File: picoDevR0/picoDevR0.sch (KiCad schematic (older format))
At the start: 10 parts, among them J1 Barrel_Jack, J2 Pico1to20, SW1 SW_Push_Dual, U1 LM1117-3.3

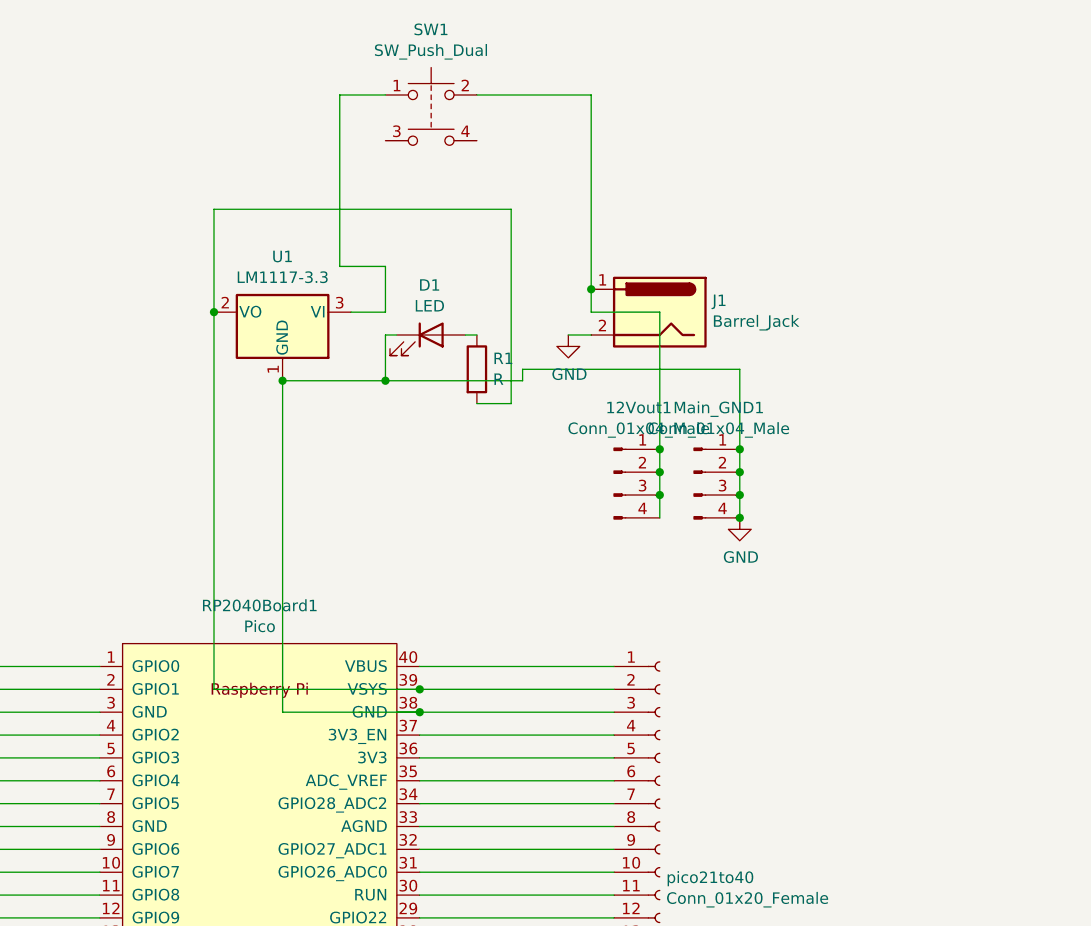
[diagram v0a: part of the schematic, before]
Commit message: added capacitors to LDO
and also made the sch more neat by adding 5V, 12V and GND labels.
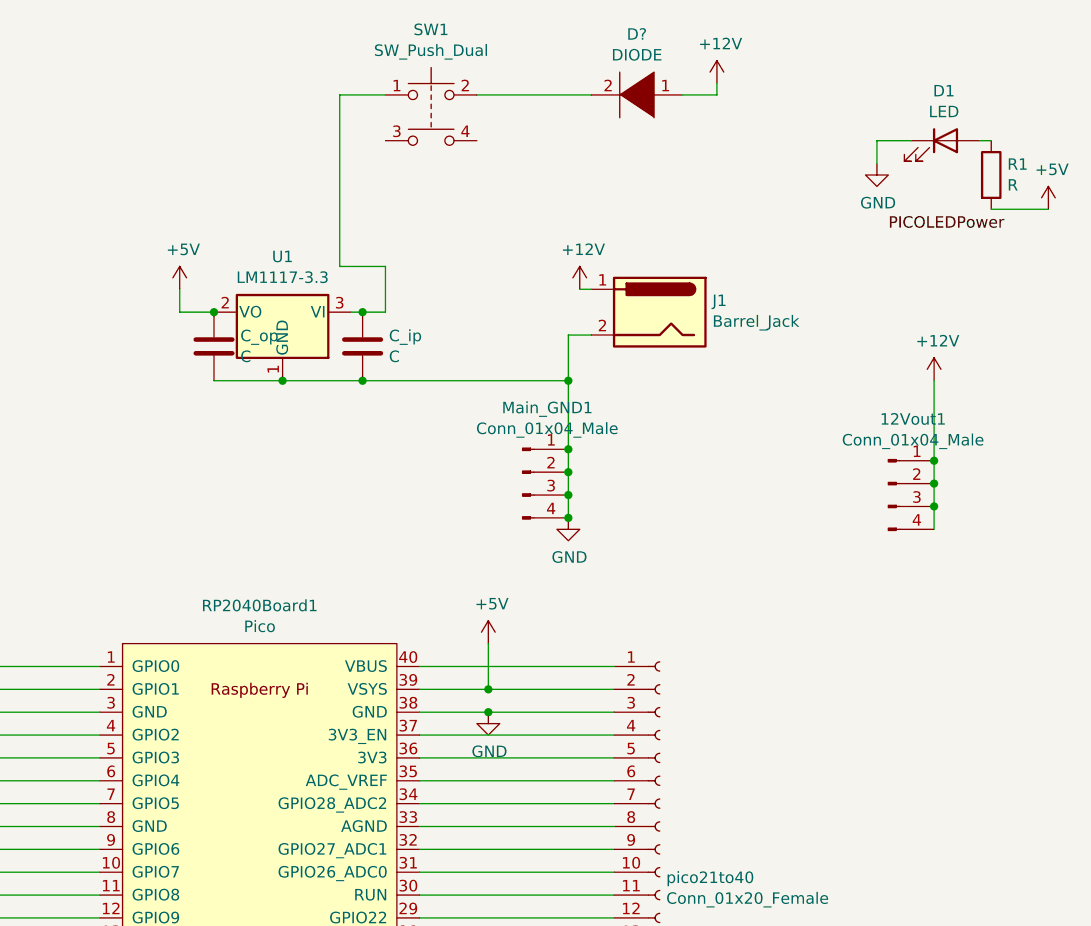
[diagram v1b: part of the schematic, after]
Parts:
- added C_ip, C_op: C, symbol Device:C
- added D?: DIODE, symbol pspice:DIODE
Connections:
- net GND: now also C_ip.2, C_op.2
- net +5V: now reaches R1.2, RP2040Board1.39 (VSYS), U1.2 (VO), pico21to40.2 (Pin_2)
- net +5V: now also C_op.1
- net at SW1.1, U1.3 (VI): now also C_ip.1
- net +12V: now reaches 12Vout1.1 (Pin_1), 12Vout1.2 (Pin_2), 12Vout1.3 (Pin_3), 12Vout1.4 (Pin_4), J1.1
- net +12V: now also D?.1 (K); no longer SW1.2
- new net: D?.2 (A), SW1.2
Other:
- moved on the sheet: 12Vout1, D1, Main_GND1, R1

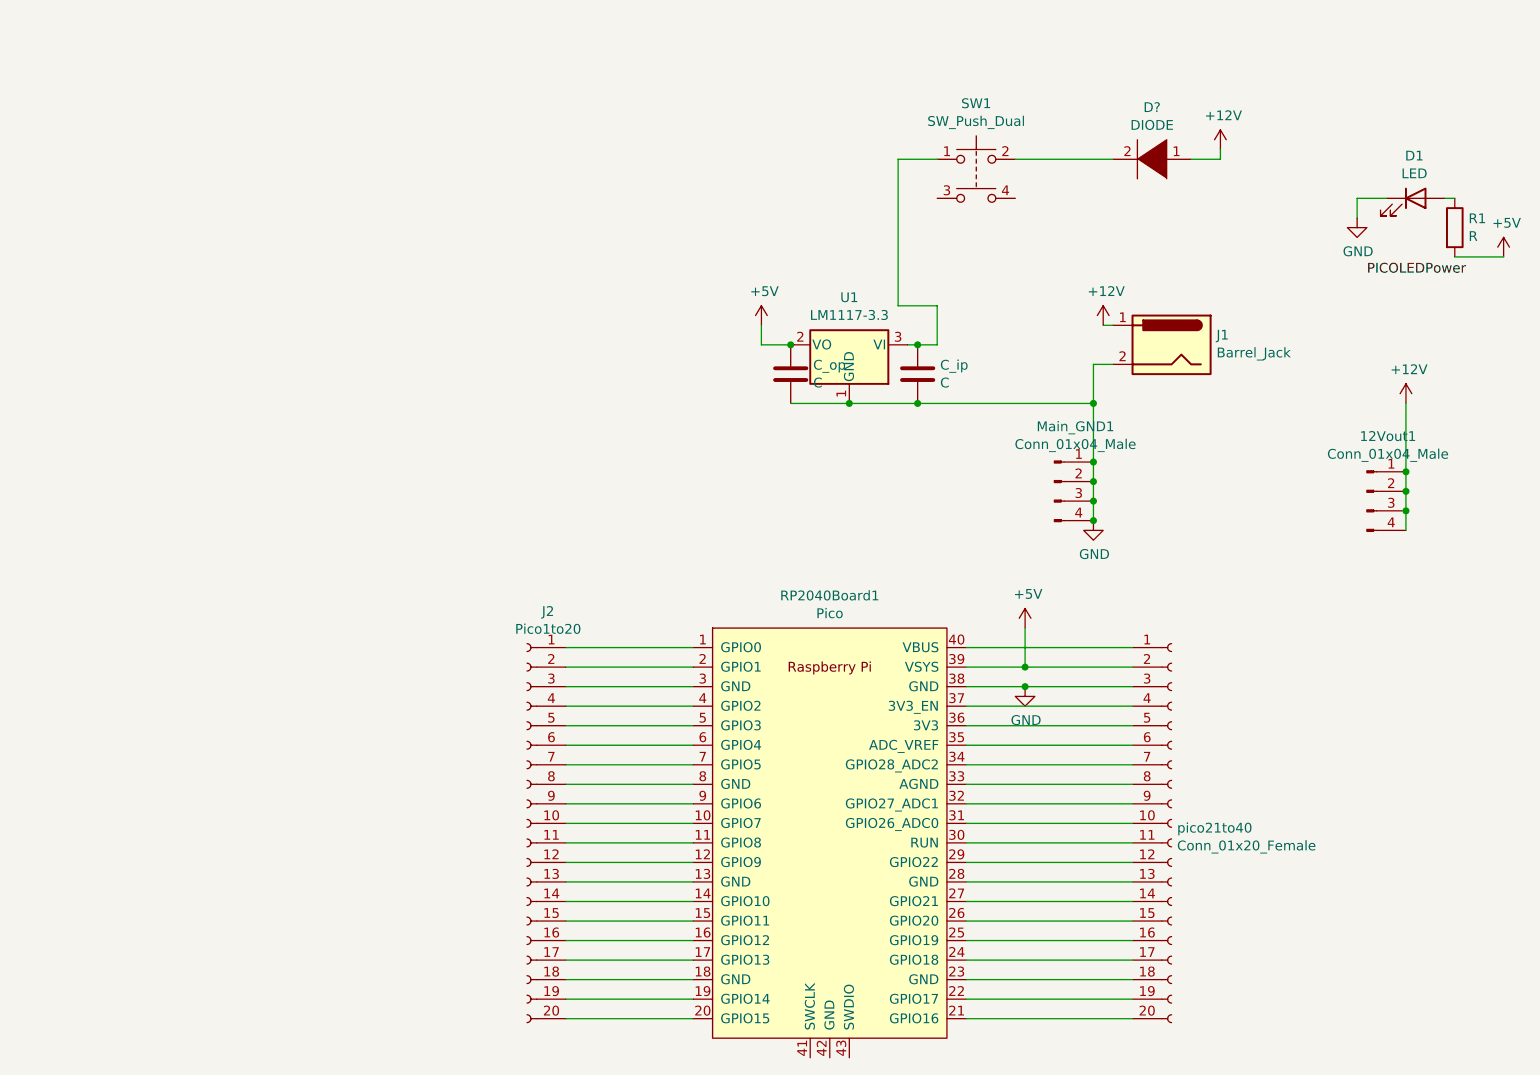
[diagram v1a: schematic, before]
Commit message: added 3v3 and 5V seperate LMs
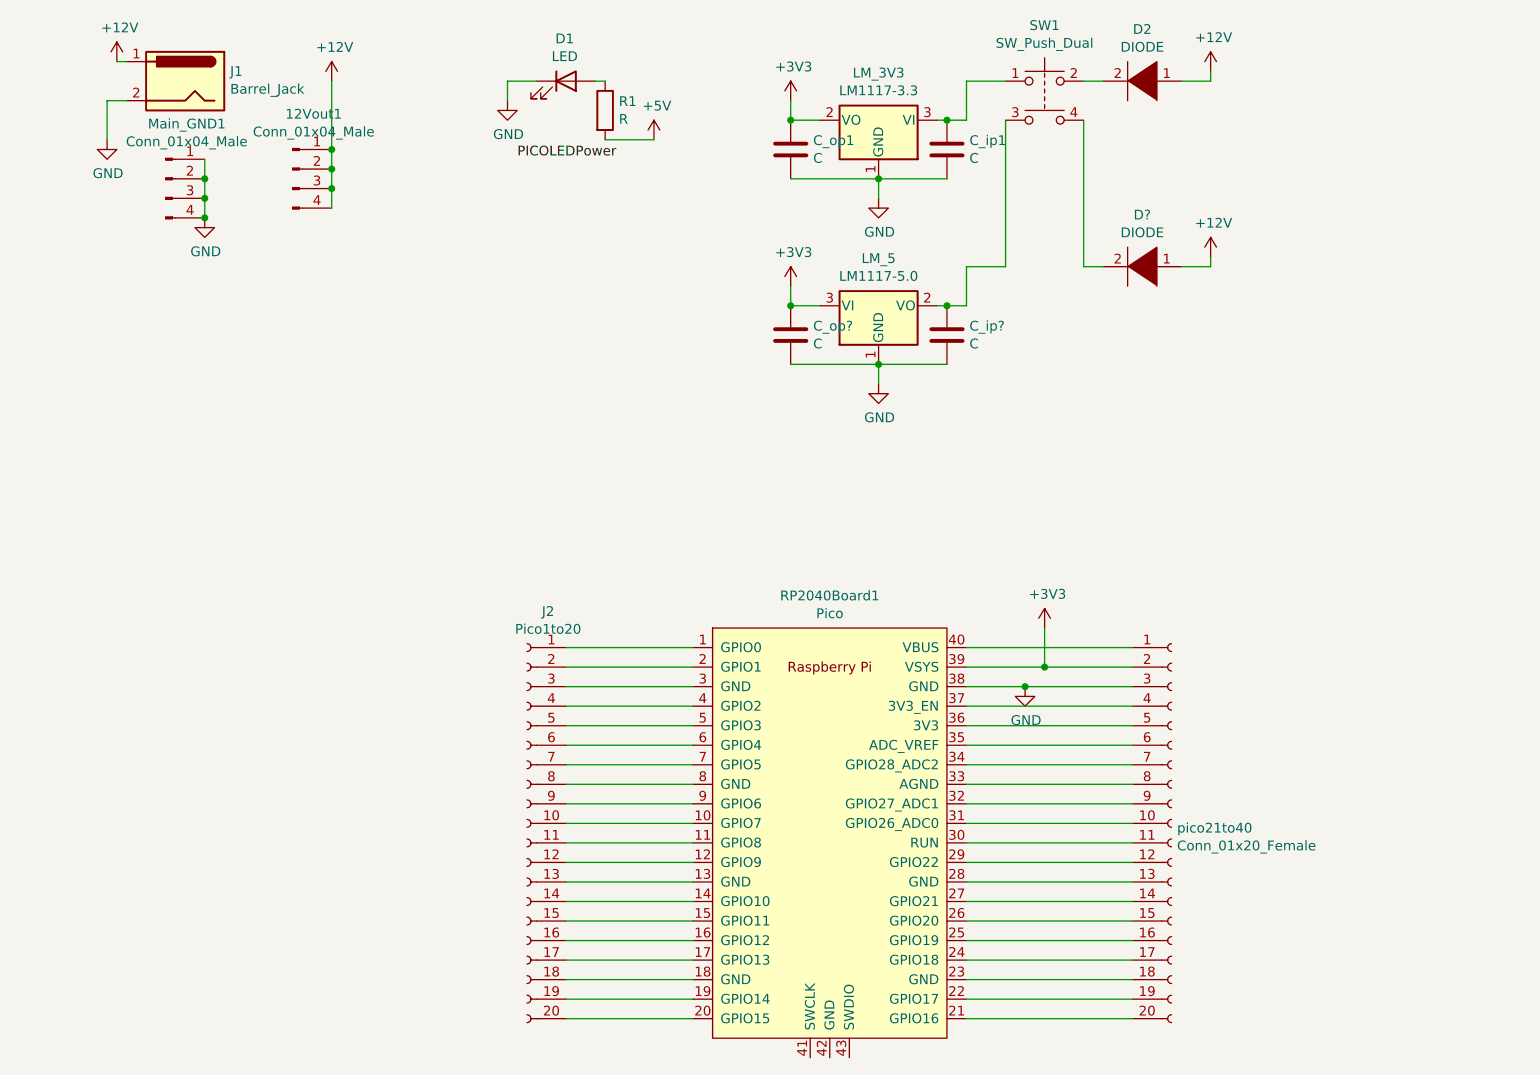
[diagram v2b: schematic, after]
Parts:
- added C_ip?, C_op?: C, Capacitor_THT:CP_Radial_D10.0mm_P2.50mm, symbol Device:C
- added D?: DIODE, Diode_THT:D_5W_P10.16mm_Horizontal, symbol pspice:DIODE
- added LM_5: LM1117-5.0, symbol Regulator_Linear:LM1117-5.0
- C_ip1: renamed from C_ip; footprint (none) -> Capacitor_THT:CP_Radial_D10.0mm_P2.50mm
- C_op1: renamed from C_op; footprint (none) -> Capacitor_THT:CP_Radial_D10.0mm_P2.50mm
- D2: renamed from D?; footprint (none) -> Diode_THT:D_5W_P10.16mm_Horizontal
- renumbered U1 to LM_3V3
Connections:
- net +12V: now also D?.1 (K)
- net +5V: no longer C_op1.1, LM_3V3.2 (VO), RP2040Board1.39 (VSYS), pico21to40.2 (Pin_2)
- net GND: now also C_ip?.2, C_op?.2, LM_5.1 (GND)
- net at SW1.3: now also C_ip?.1, LM_5.2 (VO)
- net at SW1.4: now also D?.2 (A)
- new net +3V3: C_op1.1, C_op?.1, LM_3V3.2 (VO), LM_5.3 (VI), RP2040Board1.39 (VSYS), pico21to40.2 (Pin_2)
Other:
- moved on the sheet: 12Vout1, C_ip1, C_op1, D1, D2, J1, LM_3V3, Main_GND1, R1, SW1
